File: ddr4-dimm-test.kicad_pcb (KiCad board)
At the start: 2 copper layers, 133.3 x 31.2 mm, 137 parts

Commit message: Added ECC?
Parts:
- added R126: 240Ω, Resistor_SMD:R_0402_1005Metric, F.Cu at (117.8, 102.0)
- added R127: 15Ω, Resistor_SMD:R_0402_1005Metric, F.Cu at (119.5, 106.3)
- added R128: 15Ω, Resistor_SMD:R_0402_1005Metric, F.Cu at (120.3, 106.3)
- added R129: 15Ω, Resistor_SMD:R_0402_1005Metric, F.Cu at (125.5, 106.3)
- added R130: 15Ω, Resistor_SMD:R_0402_1005Metric, F.Cu at (126.3, 106.3)
- added R131: 15Ω, Resistor_SMD:R_0402_1005Metric, F.Cu at (117.8, 106.3)
- added R132: 15Ω, Resistor_SMD:R_0402_1005Metric, F.Cu at (118.7, 106.3)
- added R133: 15Ω, Resistor_SMD:R_0402_1005Metric, F.Cu at (123.8, 106.3)
- added R134: 15Ω, Resistor_SMD:R_0402_1005Metric, F.Cu at (124.6, 106.3)
- added R135: 15Ω, Resistor_SMD:R_0402_1005Metric, F.Cu at (122.0, 106.3)
- added R136: 15Ω, Resistor_SMD:R_0402_1005Metric, F.Cu at (122.9, 106.3)
- added R137: 15Ω, Resistor_SMD:R_0402_1005Metric, F.Cu at (121.2, 106.3)
- added WAM9: DDR4-BGA78, A_my_stuff:DDR4-BGA78, F.Cu at (122.5, 97.5)
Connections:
- GF1 pad 192: unconnected-(GF1-CB5-Pad192) -> Net-(GF1-CB5)
- GF1 pad 194: unconnected-(GF1-CB1-Pad194) -> Net-(GF1-CB1)
- GF1 pad 196: unconnected-(GF1-DQS8--Pad196) -> /R_DQS8-
- GF1 pad 197: unconnected-(GF1-DQS8+-Pad197) -> /R_DQS8+
- GF1 pad 199: unconnected-(GF1-CB7-Pad199) -> Net-(GF1-CB7)
- GF1 pad 201: unconnected-(GF1-CB3-Pad201) -> Net-(GF1-CB3)
- GF1 pad 47: unconnected-(GF1-CB4-Pad47) -> Net-(GF1-CB4)
- GF1 pad 49: unconnected-(GF1-CB0-Pad49) -> Net-(GF1-CB0)
- GF1 pad 51: unconnected-(GF1-(T)DQS17+-Pad51) -> /R_DM8
- GF1 pad 54: unconnected-(GF1-CB6-Pad54) -> Net-(GF1-CB6)
- GF1 pad 56: unconnected-(GF1-CB2-Pad56) -> Net-(GF1-CB2)
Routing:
- net /R_DQS0-: track 0.00 -> 3.69 mm, vias 0 -> 1
- net /R_DQS0+: track 0.00 -> 3.69 mm, vias 0 -> 1
- net /R_DM0: track 0.00 -> 3.33 mm
- net Net-(GF1-DQ6): track 0.00 -> 3.33 mm
- net Net-(GF1-DQ1): track 0.00 -> 3.33 mm, vias 0 -> 1
- net Net-(GF1-DQ0): track 3.33 -> 4.89 mm

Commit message: kangaroo for some reason
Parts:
- C1: value 0.01uF -> 0.1uF
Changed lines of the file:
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@@
 		(sheetname "Root")
 		(sheetfile "ddr4-dimm-test.kicad_sch")
-		(attr smd)
+		(attr smd dnp)
 		(fp_line
 			(start -0.153641 0.38)
@@
 		(sheetname "Root")
 		(sheetfile "ddr4-dimm-test.kicad_sch")
-		(attr smd)
+		(attr smd dnp)
 		(fp_line
 			(start -0.153641 -0.38)
@@
 		(sheetname "Root")
 		(sheetfile "ddr4-dimm-test.kicad_sch")
-		(attr smd)
+		(attr smd dnp)
 		(fp_line
 			(start -0.153641 -0.38)
@@
 		(sheetname "Root")
 		(sheetfile "ddr4-dimm-test.kicad_sch")
-		(attr smd)
+		(attr smd dnp)
 		(fp_line
 			(start -0.153641 0.38)
@@
 		(sheetname "Root")
 		(sheetfile "ddr4-dimm-test.kicad_sch")
-		(attr smd)
+		(attr smd dnp)
 		(fp_line
 			(start -0.153641 0.38)
@@
 		(sheetname "Root")
 		(sheetfile "ddr4-dimm-test.kicad_sch")
-		(attr smd)
+		(attr smd dnp)
 		(fp_line
 			(start -0.153641 0.38)
@@
 		(sheetname "Root")
 		(sheetfile "ddr4-dimm-test.kicad_sch")
-		(attr smd)
+		(attr smd dnp)
 		(fp_line
 			(start -0.153641 0.38)
@@
 		(sheetname "Root")
 		(sheetfile "ddr4-dimm-test.kicad_sch")
-		(attr smd)
+		(attr smd dnp)
 		(fp_line
 			(start -0.153641 -0.38)
@@
 		(sheetname "Root")
 		(sheetfile "ddr4-dimm-test.kicad_sch")
-		(attr smd)
+		(attr smd dnp)
 		(fp_line
 			(start -0.153641 -0.38)
@@
 		(sheetname "Root")
 		(sheetfile "ddr4-dimm-test.kicad_sch")
-		(attr smd)
+		(attr smd dnp)
 		(fp_line
 			(start -0.153641 -0.38)
@@
 		(sheetname "Root")
 		(sheetfile "ddr4-dimm-test.kicad_sch")
-		(attr smd)
+		(attr smd dnp)
 		(fp_line
 			(start -0.153641 0.38)
@@
 		(sheetname "Root")
 		(sheetfile "ddr4-dimm-test.kicad_sch")
-		(attr smd)
+		(attr smd dnp)
 		(fp_line
 			(start -0.153641 0.38)
@@
 		(sheetname "Root")
 		(sheetfile "ddr4-dimm-test.kicad_sch")
-		(attr smd)
+		(attr smd dnp)
 		(fp_line
 			(start 3.763001 -5.5)
@@
 			)
 		)
-		(property "Value" "0.01uF"
+		(property "Value" "0.1uF"
 			(at 0 1.16 0)
 			(layer "F.Fab")
@@
 		)
 	)
+	(gr_poly
+		(pts
+			(xy 131.159849 55.749242) (xy 134.259849 57.599242) (xy 137.225 59.85) (xy 141.025 61.775) (xy 143.2 59.425)
+			(xy 144.784849 58.474242) (xy 150.325 59.25) (xy 151.475 58.175) (xy 148.05 57.7) (xy 150.525 57.275)
+			(xy 149.475 56.35) (xy 150.075 55.325) (xy 152.15 56.5) (xy 151.8 57.15) (xy 154.875 57.175) (xy 157.925 60.15)
+			(xy 153.625 58.95) (xy 151.175 63.175) (xy 150.034849 62.599242) (xy 149.409849 63.524242) (xy 150.184849 64.224242)
+			(xy 149.534849 64.424242) (xy 148.209849 62.574242) (xy 146.884849 62.524242) (xy 146.609849 64.924242)
+			(xy 144.784849 67.174242) (xy 148.709849 69.799242) (xy 141.2 68.9) (xy 140.95 65.4) (xy 134.9 63.175)
+		)
+		(stroke
+			(width 0.05)
+			(type solid)
+		)
+		(fill none)
+		(layer "User.1")
+	)
 	(gr_line

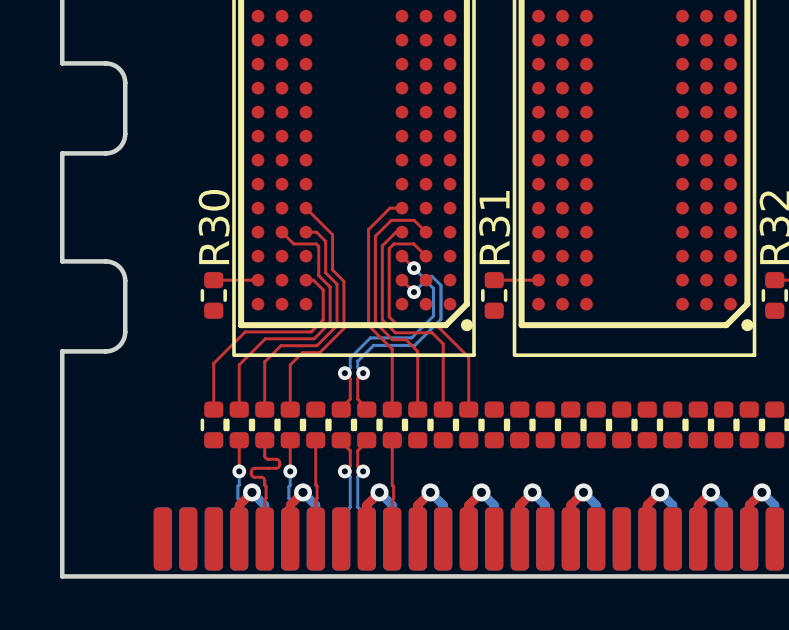
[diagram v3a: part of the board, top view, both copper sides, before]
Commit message: Tried some data bus length matching
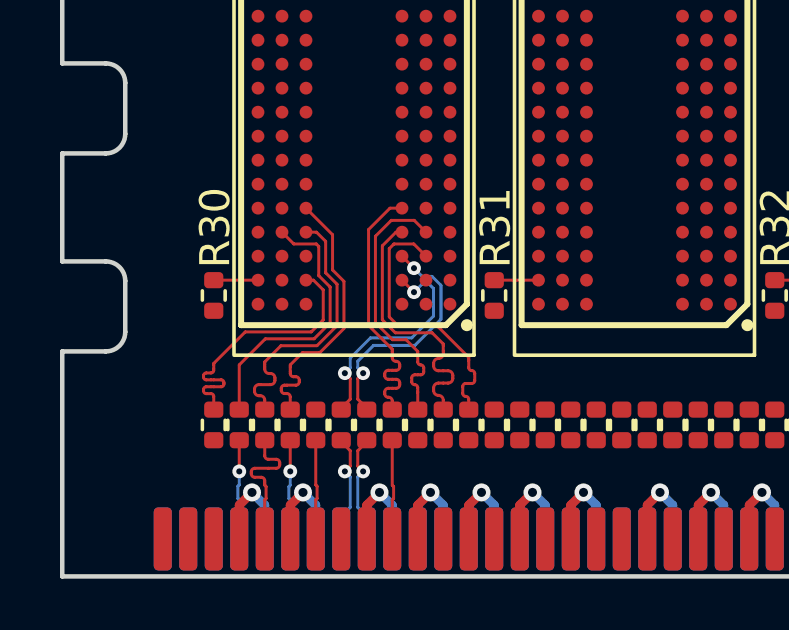
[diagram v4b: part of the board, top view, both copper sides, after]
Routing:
- net DQ4: track 7.50 -> 9.19 mm
- net DQ6: track 7.74 -> 9.18 mm
- net DQ2: track 7.86 -> 9.18 mm
- net DQ0: track 8.25 -> 9.19 mm
- net DQ1: track 8.32 -> 9.20 mm
- net DQ3: track 8.68 -> 9.20 mm
- net DQ7: track 8.69 -> 9.21 mm

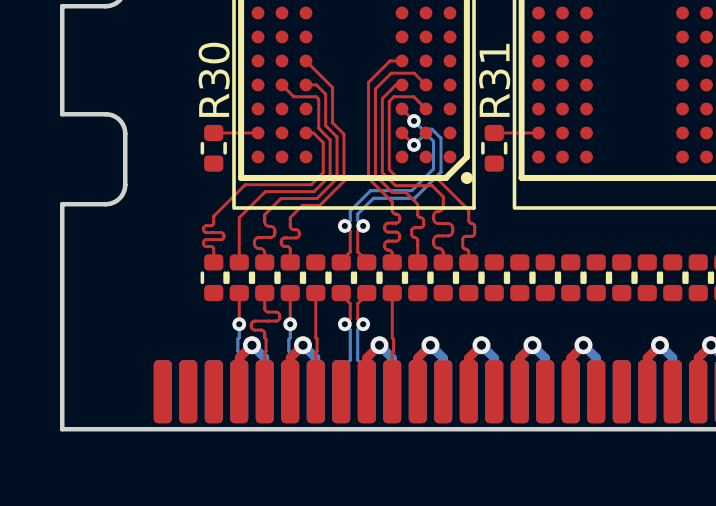
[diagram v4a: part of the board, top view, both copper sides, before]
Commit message: Changed to 6 layer
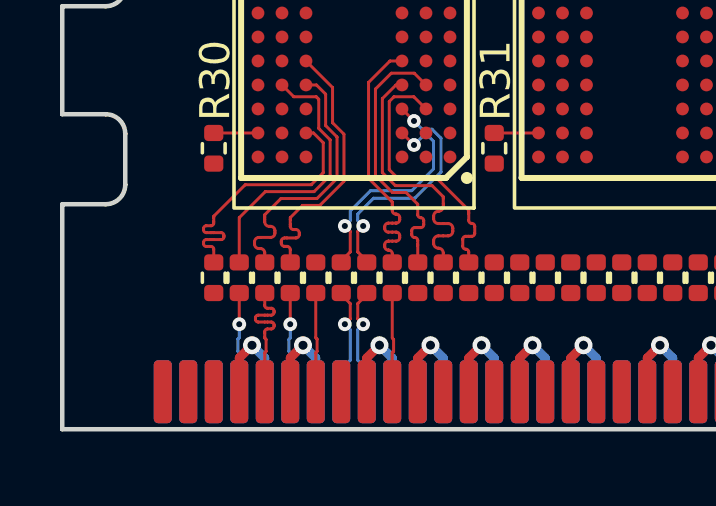
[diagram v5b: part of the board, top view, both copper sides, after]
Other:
- copper layers 2 -> 6
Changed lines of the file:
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@@
 	(layers
 		(0 "F.Cu" signal)
+		(1 "In1.Cu" signal)
+		(2 "In2.Cu" signal)
+		(3 "In3.Cu" signal)
+		(4 "In4.Cu" signal)
 		(31 "B.Cu" signal)
 		(32 "B.Adhes" user "B.Adhesive")
@@
 			)
 			(layer "dielectric 1"
+				(type "prepreg")
+				(thickness 0.1)
+				(material "FR4")
+				(epsilon_r 4.5)
+				(loss_tangent 0.02)
+			)
+			(layer "In1.Cu"
+				(type "copper")
+				(thickness 0.035)
+			)
+			(layer "dielectric 2"
+				(type "core")
+				(thickness 0.535)
+				(material "FR4")
+				(epsilon_r 4.5)
+				(loss_tangent 0.02)
+			)
+			(layer "In2.Cu"
+				(type "copper")
+				(thickness 0.035)
+			)
+			(layer "dielectric 3"
+				(type "prepreg")
+				(thickness 0.1)
+				(material "FR4")
+				(epsilon_r 4.5)
+				(loss_tangent 0.02)
+			)
+			(layer "In3.Cu"
+				(type "copper")
+				(thickness 0.035)
+			)
+			(layer "dielectric 4"
 				(type "core")
-				(thickness 1.51)
+				(thickness 0.535)
+				(material "FR4")
+				(epsilon_r 4.5)
+				(loss_tangent 0.02)
+			)
+			(layer "In4.Cu"
+				(type "copper")
+				(thickness 0.035)
+			)
+			(layer "dielectric 5"
+				(type "prepreg")
+				(thickness 0.1)
 				(material "FR4")
 				(epsilon_r 4.5)
@@
 	)
 	(segment
-		(start 82.22 107.795)
-		(end 81.77 107.795)
+		(start 82.318 108.057)
+		(end 82.192 108.057)
 		(width 0.1)
 		(layer "F.Cu")
@@
 	)
 	(segment
-		(start 82.1 108.85)
-		(end 82.1 110.15)
+		(start 82.145 108.405319)
+		(end 82.145 108.805)
 		(width 0.1)
 		(layer "F.Cu")
@@
 	)
 	(segment
-		(start 82.48 107.795)
-		(end 82.22 107.795)
+		(start 82.1 108.195)
+		(end 82.1 108.325)
 		(width 0.1)
 		(layer "F.Cu")
@@
 	)
 	(segment
-		(start 82.145 108.405319)
-		(end 82.145 108.805)
+		(start 81.79 107.689)
+		(end 81.79 107.735)
 		(width 0.1)
 		(layer "F.Cu")
@@
 	)
 	(segment
-		(start 82.1 108.215)
-		(end 82.1 108.275)
+		(start 82.318 107.597)
+		(end 82.192 107.597)
 		(width 0.1)
 		(layer "F.Cu")
@@
 	)
 	(segment
-		(start 82.6 107.615)
-		(end 82.6 107.675)
+		(start 82.192 107.597)
+		(end 82.1 107.597)
 		(width 0.1)
 		(layer "F.Cu")
@@
 	)
 	(segment
-		(start 82.1 106.860001)
-		(end 82.1 107.375)
+		(start 82.41 107.919)
+		(end 82.41 107.965)
 		(width 0.1)
 		(layer "F.Cu")
@@
 	)
 	(segment
-		(start 82.22 107.495)
-		(end 82.48 107.495)
+		(start 82.1 108.325)
+		(end 82.1 108.360319)
 		(width 0.1)
 		(layer "F.Cu")
@@
 	)
 	(segment
-		(start 82.1 108.325)
-		(end 82.1 108.360319)
+		(start 82.1 107.827)
+		(end 82.192 107.827)
 		(width 0.1)
 		(layer "F.Cu")
@@
 	)
 	(segment
-		(start 82.145 108.805)
-		(end 82.1 108.85)
+		(start 82.192 107.367)
+		(end 82.318 107.367)
 		(width 0.1)
 		(layer "F.Cu")
@@
 	)
 	(segment
-		(start 81.77 108.095)
-		(end 81.98 108.095)
+		(start 82.1 108.149)
+		(end 82.1 108.195)
+		(width 0.1)
+		(layer "F.Cu")
+		(net 71)
+	)
+	(segment
+		(start 82.1 108.85)
+		(end 82.1 110.15)
+		(width 0.1)
+		(layer "F.Cu")
+		(net 71)
+	)
+	(segment
+		(start 82.1 107.597)
+		(end 81.882 107.597)
+		(width 0.1)
+		(layer "F.Cu")
+		(net 71)
+	)
+	(segment
+		(start 81.882 107.827)
+		(end 82.1 107.827)
 		(width 0.1)
 		(layer "F.Cu")
@@
 	)
 	(segment
-		(start 82.1 108.275)
-		(end 82.1 108.325)
+		(start 82.145 108.805)
+		(end 82.1 108.85)
 		(width 0.1)
 		(layer "F.Cu")
@@
 	)
 	(segment
-		(start 81.65 107.915)
-		(end 81.65 107.975)
+		(start 82.41 107.459)
+		(end 82.41 107.505)
+		(width 0.1)
+		(layer "F.Cu")
+		(net 71)
+	)
+	(segment
+		(start 82.192 107.827)
+		(end 82.318 107.827)
+		(width 0.1)
+		(layer "F.Cu")
+		(net 71)
+	)
+	(segment
+		(start 82.1 106.860001)
+		(end 82.1 107.275)
 		(width 0.1)
 		(layer "F.Cu")
@@
 	)
 	(arc
-		(start 81.77 107.795)
-		(mid 81.685147 107.830147)
-		(end 81.65 107.915)
+		(start 82.1 107.275)
+		(mid 82.126946 107.340054)
+		(end 82.192 107.367)
 		(width 0.1)
 		(layer "F.Cu")
@@
 	)
 	(arc
-		(start 82.48 107.495)
-		(mid 82.564853 107.530147)
-		(end 82.6 107.615)
+		(start 81.882 107.597)
+		(mid 81.816946 107.623946)
+		(end 81.79 107.689)
 		(width 0.1)
 		(layer "F.Cu")
@@
 	)
 	(arc
-		(start 82.6 107.675)
-		(mid 82.564853 107.759853)
-		(end 82.48 107.795)
+		(start 82.41 107.505)
+		(mid 82.383054 107.570054)
+		(end 82.318 107.597)
 		(width 0.1)
 		(layer "F.Cu")
@@
 	)
 	(arc
-		(start 81.98 108.095)
-		(mid 82.064853 108.130147)
-		(end 82.1 108.215)
+		(start 82.318 107.367)
+		(mid 82.383054 107.393946)
+		(end 82.41 107.459)
 		(width 0.1)
 		(layer "F.Cu")
@@
 	)
 	(arc
-		(start 82.1 107.375)
-		(mid 82.135147 107.459853)
-		(end 82.22 107.495)
+		(start 82.318 107.827)
+		(mid 82.383054 107.853946)
+		(end 82.41 107.919)
 		(width 0.1)
 		(layer "F.Cu")
@@
 	)
 	(arc
-		(start 81.65 107.975)
-		(mid 81.685147 108.059853)
-		(end 81.77 108.095)
+		(start 82.192 108.057)
+		(mid 82.126946 108.083946)
+		(end 82.1 108.149)
+		(width 0.1)
+		(layer "F.Cu")
+		(net 71)
+	)
+	(arc
+		(start 82.41 107.965)
+		(mid 82.383054 108.030054)
+		(end 82.318 108.057)
+		(width 0.1)
+		(layer "F.Cu")
+		(net 71)
+	)
+	(arc
+		(start 81.79 107.735)
+		(mid 81.816946 107.800054)
+		(end 81.882 107.827)
 		(width 0.1)
 		(layer "F.Cu")
@@
 		(base_line
 			(pts
-				(xy 82.1 107.375) (xy 82.1 108.325)
+				(xy 82.1 107.275) (xy 82.1 108.325)
 			)
 		)
@@
 		(last_status "too_short")
 		(last_track_width 0.1)
-		(last_tuning "4.9182 mm (too short)")
-		(max_amplitude 1)
+		(last_tuning "4.8714 mm (too short)")
+		(max_amplitude 0.31)
 		(min_amplitude 0.2)
-		(min_spacing 0.3)
+		(min_spacing 0.23)
 		(origin
-			(xy 82.1 107.375)
+			(xy 82.1 107.275)
 		)
 		(override_custom_rules no)
@@
 		(target_skew_min -0.1)
 		(tuning_mode "single")
-		(members 05ce82ad-b8ad-45e4-ace5-2bd449e6ef04 20a28489-34d0-496b-ab9c-a5ee74c8e733
-			20c0ccc3-7e4d-430b-a103-467b1ee3b262 25abd6a1-57d4-40c5-98b4-24b0b2c40d7c
-			33798d54-5b44-4106-a4e0-70279f473b4d 3494aea0-52bd-4aad-b5e3-21384f501ecd
-			36e75e3d-6722-46fa-a57d-89df6a8533bb 59cc611a-c35d-41a4-96b6-09d00a432a8b
-			7cfd4d45-1db8-4cad-bcb1-76d7cfbbfc44 9ed76e18-bec4-4b55-9b1a-3b0429013418
-			e9b0c1f7-33ac-4fab-b680-3762ece888d6 f198e427-9c7a-4132-ae10-670fd33da49a
-			f670c1e9-fd3b-47b4-9595-22fbbe366e25 f99c0de9-4053-4de6-b3f1-407a33e6e9a3
-		)
+		(members)
 	)
 	(generated
